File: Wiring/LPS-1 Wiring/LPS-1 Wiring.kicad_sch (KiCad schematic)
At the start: 22 parts, among them J1 Block_Connector_01_b, J10 Block_Connector_01_b, J11 Block_Connector_01_b, J12 GND Block, J13 Battery, J14 Fuse Block, J15 Solar Panel, J16 Solar charging unit, J17 LPS-1 Monitoring Unit, J2 Block_Connector_01_b, J3 Block_Connector_01_b, J4 Block_Connector_01_b, J5 Block_Connector_01_b, J6 Block_Connector_01_b, J7 Pwr Block, J8 Block_Connector_01_b, J9 Block_Connector_01_b, SW2 TRU Components NO

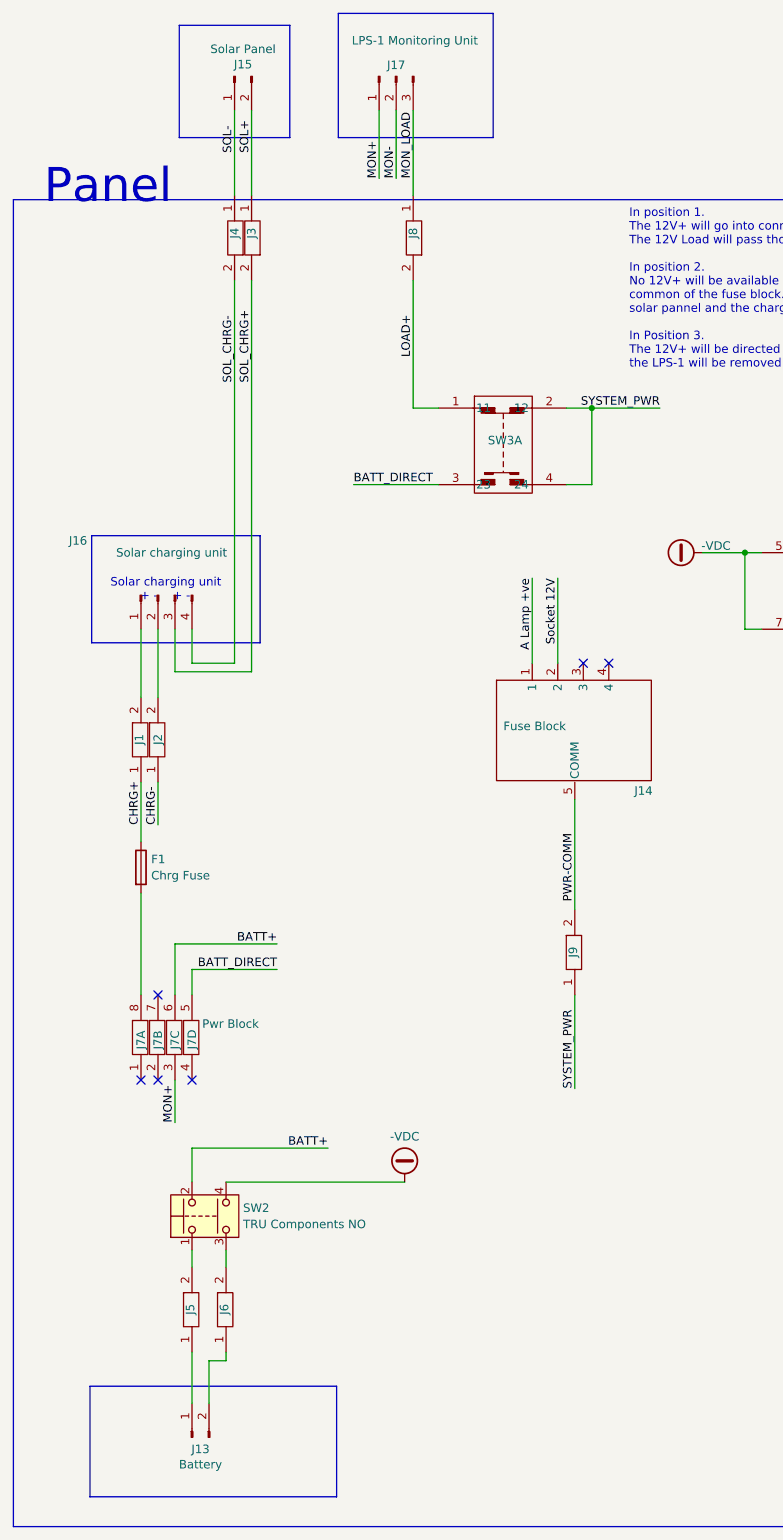
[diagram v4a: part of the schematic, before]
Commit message: Refactored the nomenclature for non-connector components
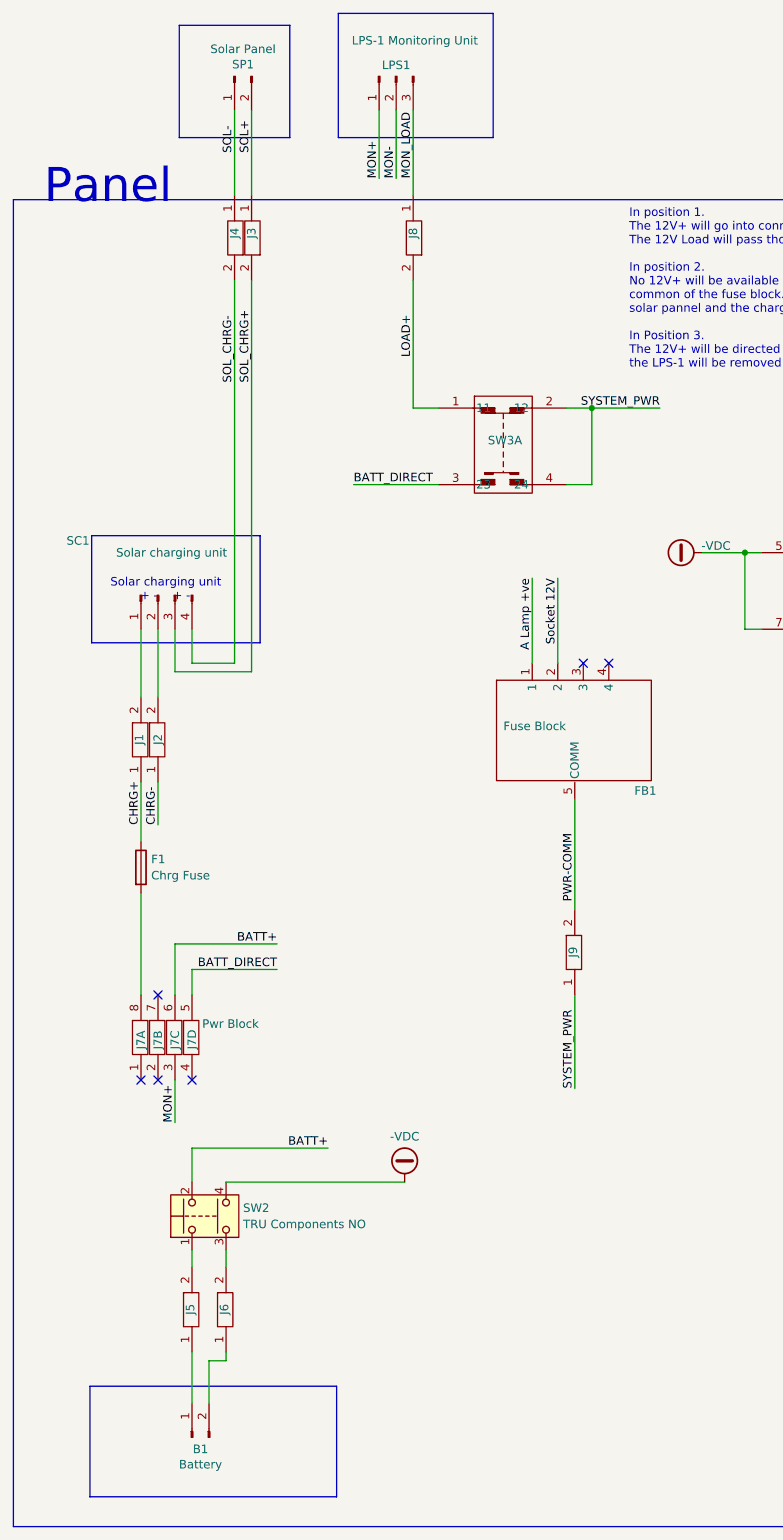
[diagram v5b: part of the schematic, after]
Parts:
- renumbered J13 to B1, J14 to FB1, J17 to LPS1, J16 to SC1, J15 to SP1
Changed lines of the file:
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@@
 		(in_pos_files yes)
 		(dnp no)
-		(property "Reference" "J16"
+		(property "Reference" "SC1"
 			(at 104.902 102.362 90)
 			(show_name no)
@@
 			(project "LPS-1 Wiring"
 				(path "/b9731cf8-57f6-454f-95de-12f1db0e3ec9"
-					(reference "J16")
+					(reference "SC1")
 					(unit 1)
 				)
@@
 		(in_pos_files yes)
 		(dnp no)
-		(property "Reference" "J14"
+		(property "Reference" "FB1"
 			(at 187.96 139.7 0)
 			(show_name no)
@@
 			(project "LPS-1 Wiring"
 				(path "/b9731cf8-57f6-454f-95de-12f1db0e3ec9"
-					(reference "J14")
+					(reference "FB1")
 					(unit 1)
 				)
@@
 		(in_pos_files yes)
 		(dnp no)
-		(property "Reference" "J17"
+		(property "Reference" "LPS1"
 			(at 152.4 31.3507 90)
 			(show_name no)
@@
 			(project "LPS-1 Wiring"
 				(path "/b9731cf8-57f6-454f-95de-12f1db0e3ec9"
-					(reference "J17")
+					(reference "LPS1")
 					(unit 1)
 				)
@@
 		(in_pos_files yes)
 		(dnp no)
-		(property "Reference" "J13"
+		(property "Reference" "B1"
 			(at 123.19 237.998 90)
 			(show_name no)
@@
 			(project "LPS-1 Wiring"
 				(path "/b9731cf8-57f6-454f-95de-12f1db0e3ec9"
-					(reference "J13")
+					(reference "B1")
 					(unit 1)
 				)
@@
 		(in_pos_files yes)
 		(dnp no)
-		(property "Reference" "J15"
+		(property "Reference" "SP1"
 			(at 129.54 31.242 90)
 			(show_name no)
@@
 			(project "LPS-1 Wiring"
 				(path "/b9731cf8-57f6-454f-95de-12f1db0e3ec9"
-					(reference "J15")
+					(reference "SP1")
 					(unit 1)
 				)

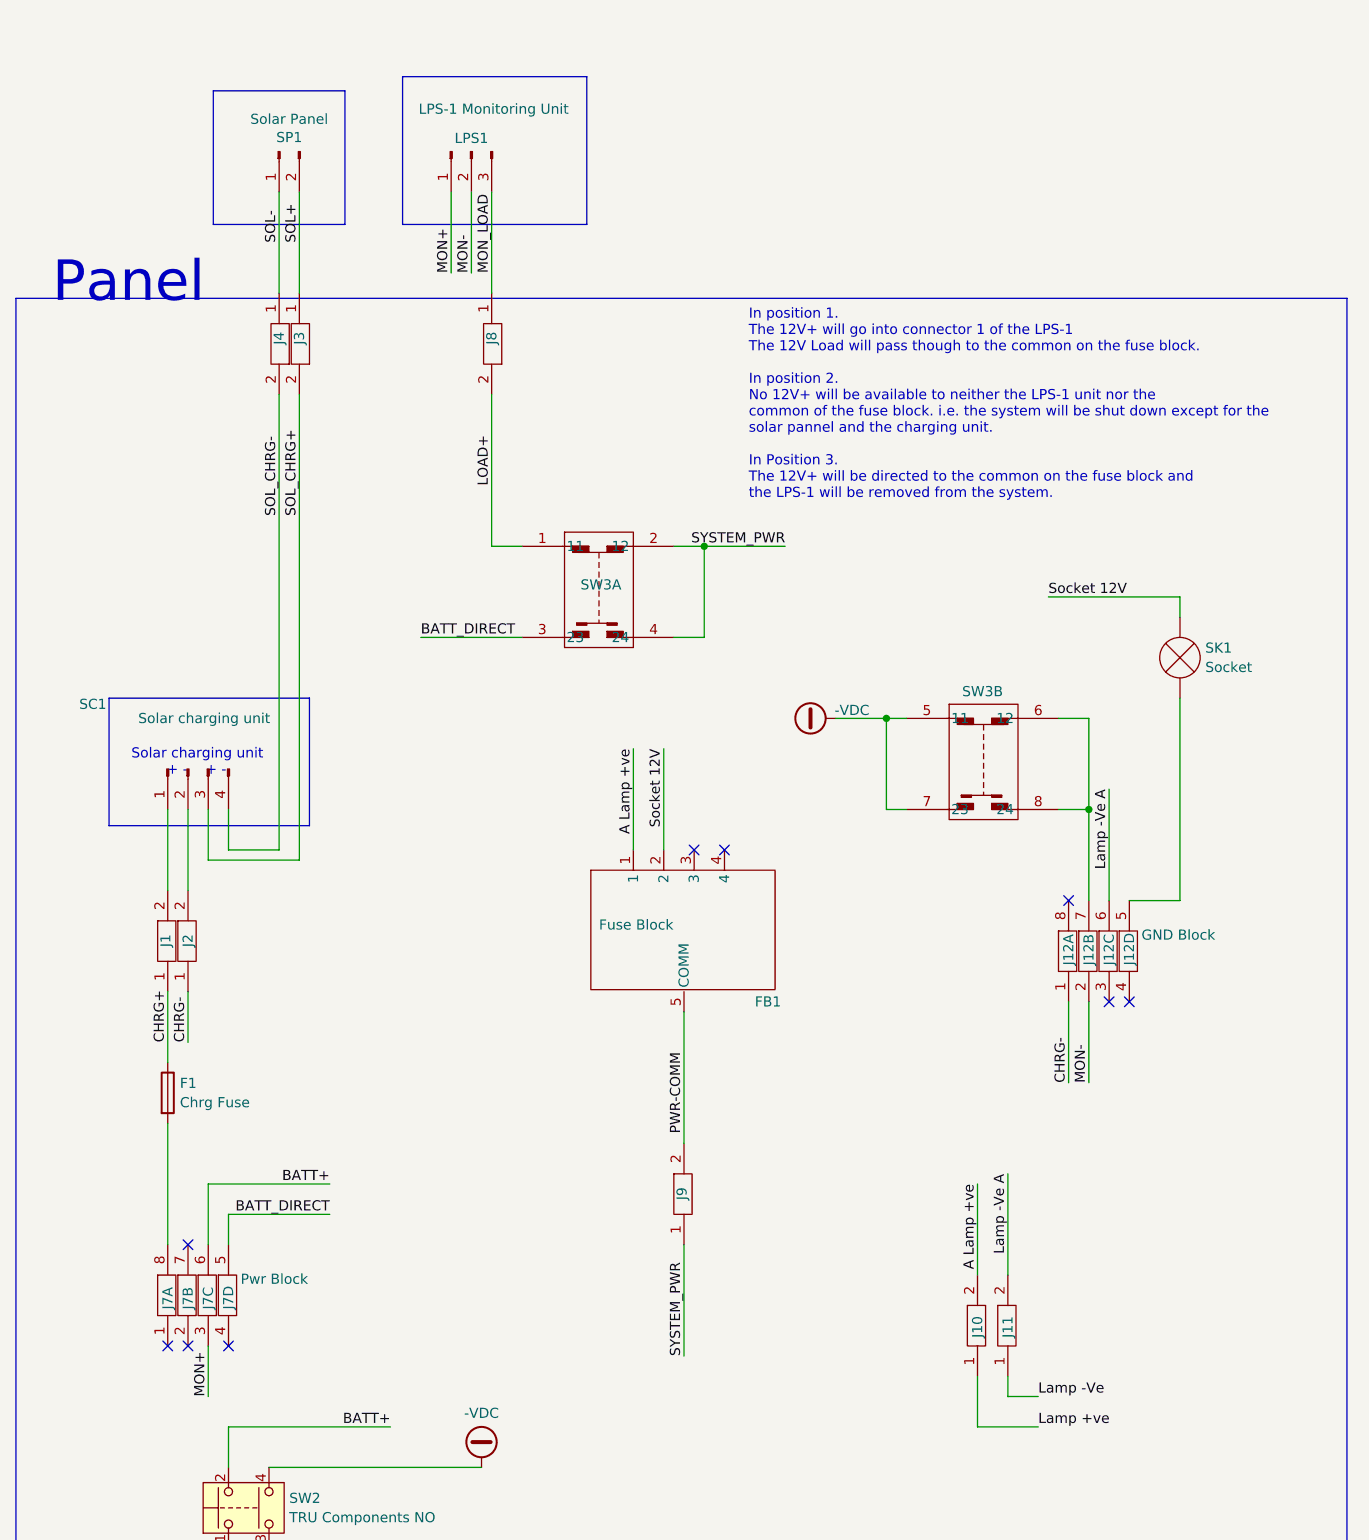
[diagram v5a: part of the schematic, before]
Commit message: Updates to the wriging layout
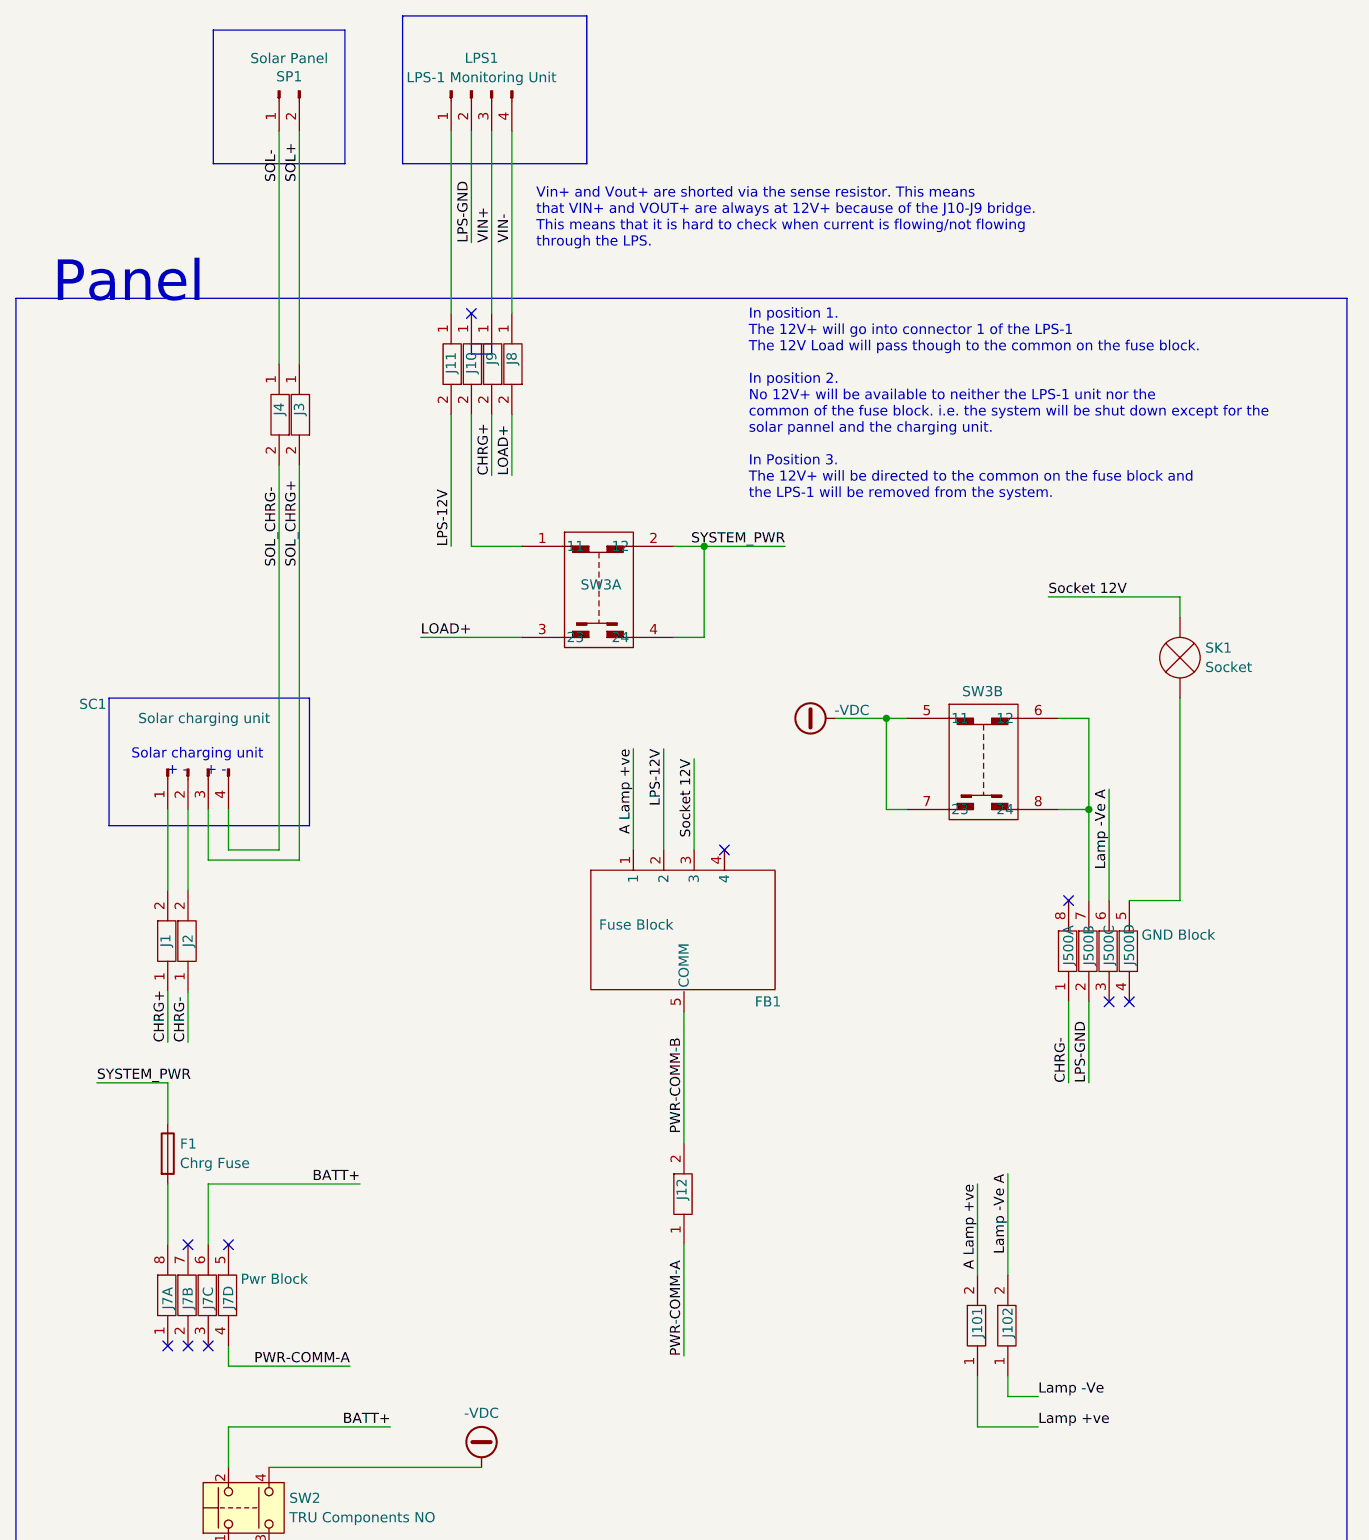
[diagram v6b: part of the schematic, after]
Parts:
- removed LPS1: LPS-1 Monitoring Unit, Wiring:LPS-1, symbol Connector:Conn_01x03_Pin
- added J10, J11, J9: Block_Connector_01_b, Wiring:Degson_01_PC2.5-01P-11-00AH-1_5.2, symbol Wiring:Block_Connector_01_Pin
- added LPS1: LPS-1 Monitoring Unit, Wiring:LPS-1_EXT_PWR, symbol Connector:Conn_01x04_Pin
- renumbered J10 to J101, J11 to J102, J9 to J12, J12 to J500
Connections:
- net CHRG+: now also J9.2; no longer F1.1
- net LOAD+: now also SW3.3 (23); no longer SW3.1 (11)
- net SYSTEM_PWR: now also F1.1; no longer J12.1
- net Socket 12V: now also FB1.3; no longer FB1.2
- net PWR-COMM-A: now reaches J7.4
- net PWR-COMM-A: now also J12.1
- net BATT_DIRECT: no longer names the net of J7.5
- net BATT_DIRECT: no longer SW3.3 (23)
- net MON+: no longer names the net of J7.3
- net MON- renamed LPS-GND
- net LPS-GND: now also LPS1.2 (Pin_2)
- net MON_LOAD renamed VIN-
- net VIN-: now also LPS1.4 (Pin_4)
- net PWR-COMM renamed PWR-COMM-B
- new net: J11.1, LPS1.1 (Pin_1)
- new net: J10.2, SW3.1 (11)
- new net LPS-12V: FB1.2, J11.2
- new net VIN+: J9.1, LPS1.3 (Pin_3)
- no-connect marks 9 -> 10
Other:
- note added: "Vin+ and Vout+ are shorted via the sense resistor. This means that VIN+ and VOUT+ are always at 12V+ because of the J10-J9 bridge. This means that it is hard to check when current is flowing/not flowing through the LPS."
- moved on the sheet: F1, J3, J4, J8, SP1
